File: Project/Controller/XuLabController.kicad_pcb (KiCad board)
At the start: 4 copper layers, 75 x 81 mm, 94 parts, among them J1 Power, J10 Servo, J11 Servo, J12 Servo, J13 Thruster, J14 I2C, J15 I2C, J16 UART1, J17 UART2, J18 SPI1, J19 SPI2, J2 SWD, J20 Interrupt, J21 Interrupt, J22 Interrupt, J3 USB_C_Receptacle_USB2.0_16P, J4 Bar30, J5 Servo, J6 Servo, J7 Servo, J8 Servo, J9 Servo, SW1 SW_SPDT, SW2 SW_SPDT, SW3 SW_Push, U1 LM66100DCK, U10 SHTC3, U2 MIC5219-3.3YM5, U3 LM66100DCK, U4 STM32F446RCTx, U5 24AA64-OT, U6 USBLC6-2SC6, U7 BMI088, U8 MMC5983MA, U9 MCP9700Ax-ETT, Y1 8MHz

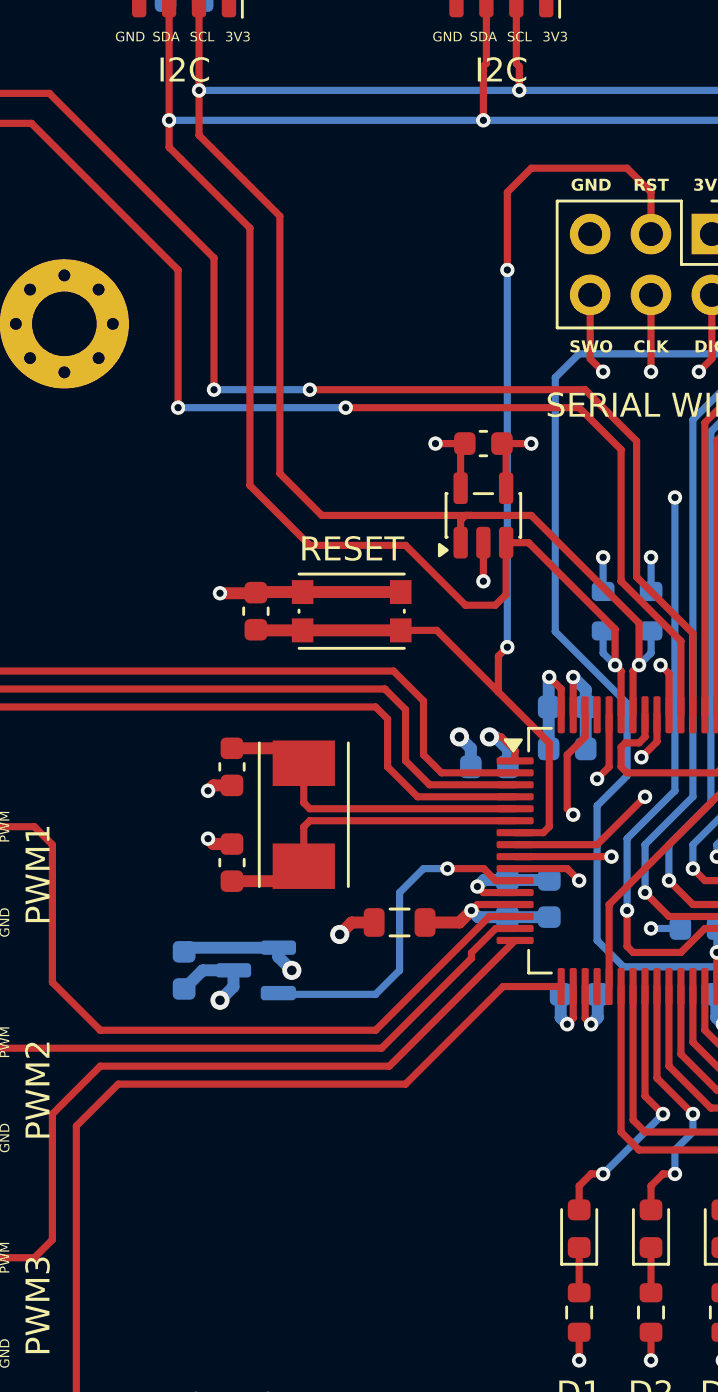
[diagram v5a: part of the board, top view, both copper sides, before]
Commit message: Move reset button to open space
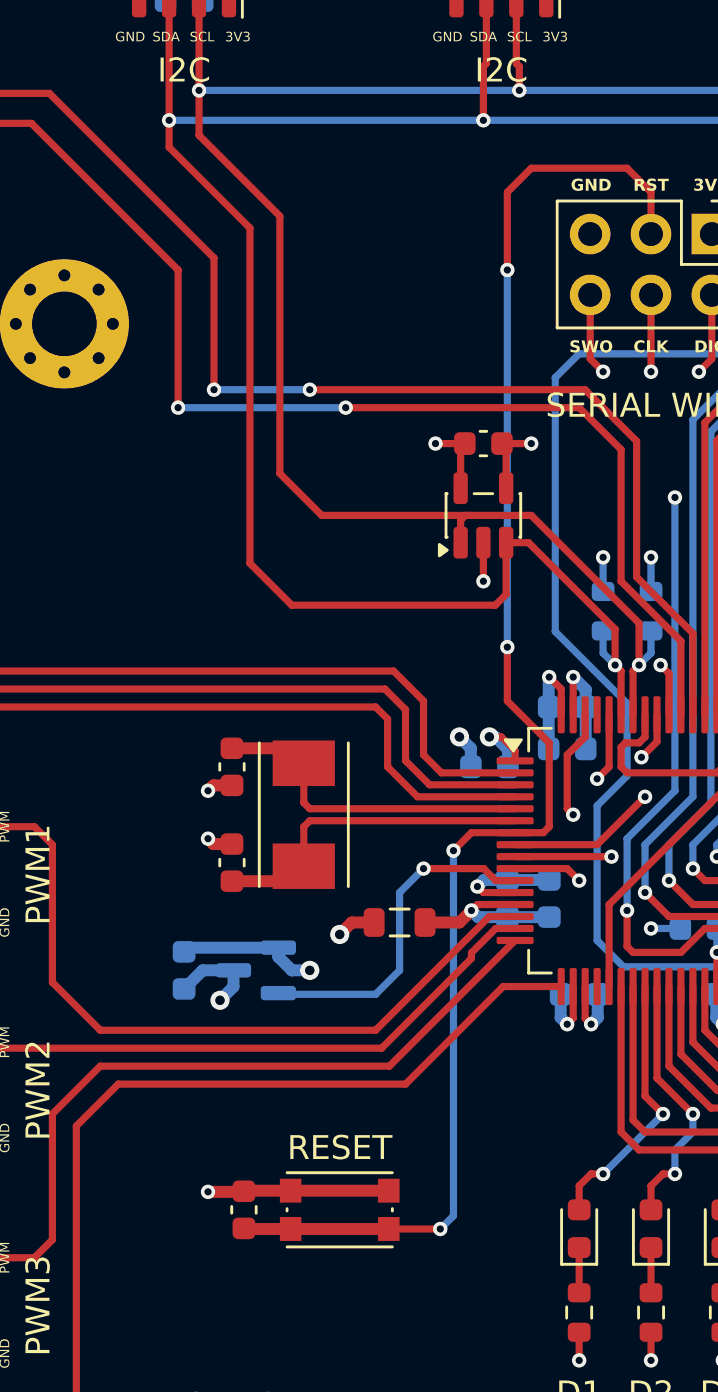
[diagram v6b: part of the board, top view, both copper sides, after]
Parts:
- moved C15 25.0 mm to (128.5, 115.0)
- moved SW3 25.0 mm to (132.5, 115.0)
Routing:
- net /Microcontroller/NRST: track 48.8 -> 64.5 mm, vias 2 -> 4
- net /I2C1_SDA: track 103.4 -> 105.3 mm
- net +3.3V: track 81.6 -> 82.4 mm

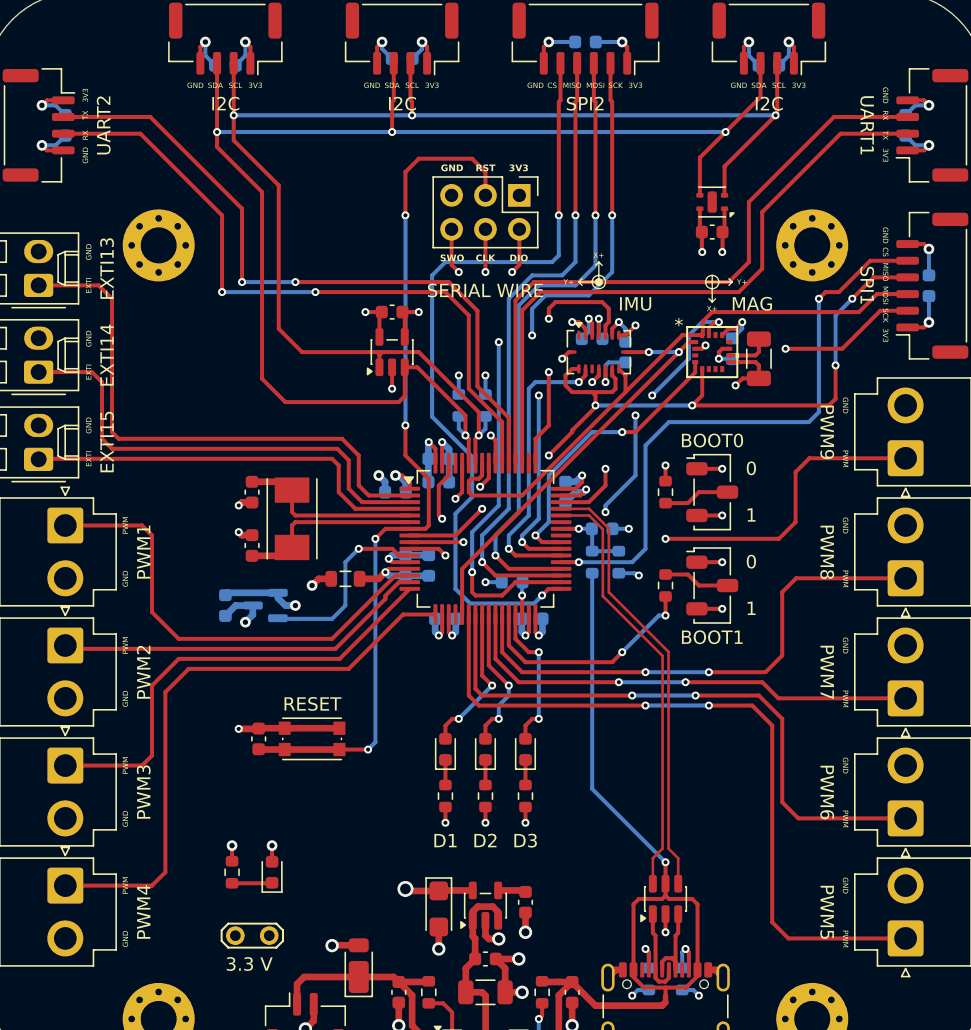
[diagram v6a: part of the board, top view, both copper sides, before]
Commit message: Reformat and remove small silkscreen
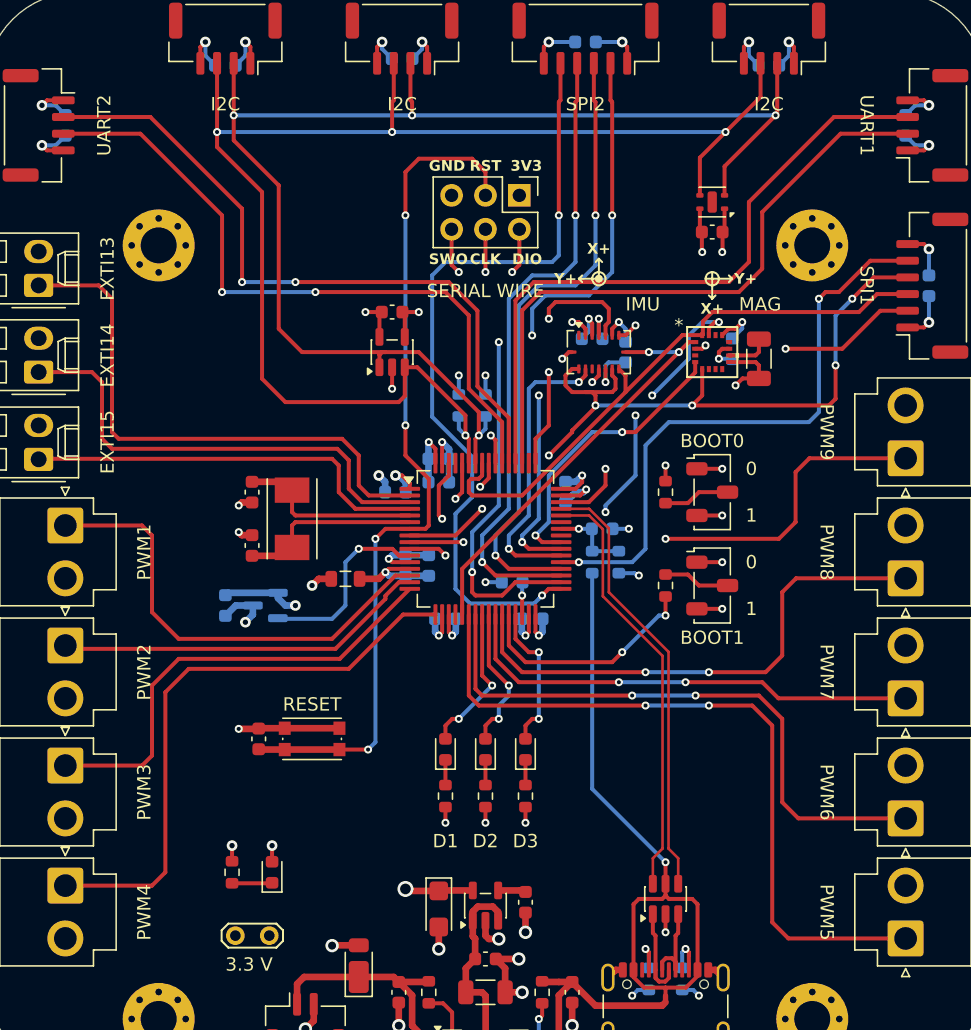
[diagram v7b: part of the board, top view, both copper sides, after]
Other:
- board text removed: "CS"
- board text removed: "EXTI"
- board text removed: "MISO"
- board text removed: "MOSI"
- board text removed: "PWM"
- board text removed: "RX"
- board text removed: "SCK"
- board text removed: "SCL"
- board text removed: "SDA"
- board text removed: "TX"
